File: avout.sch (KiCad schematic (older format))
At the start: 53 parts, among them CN6 AUDIO_VIDEO, M1 Modulator, Q3 2SC1815, Q81 2SC1815, Q82 2SC1815

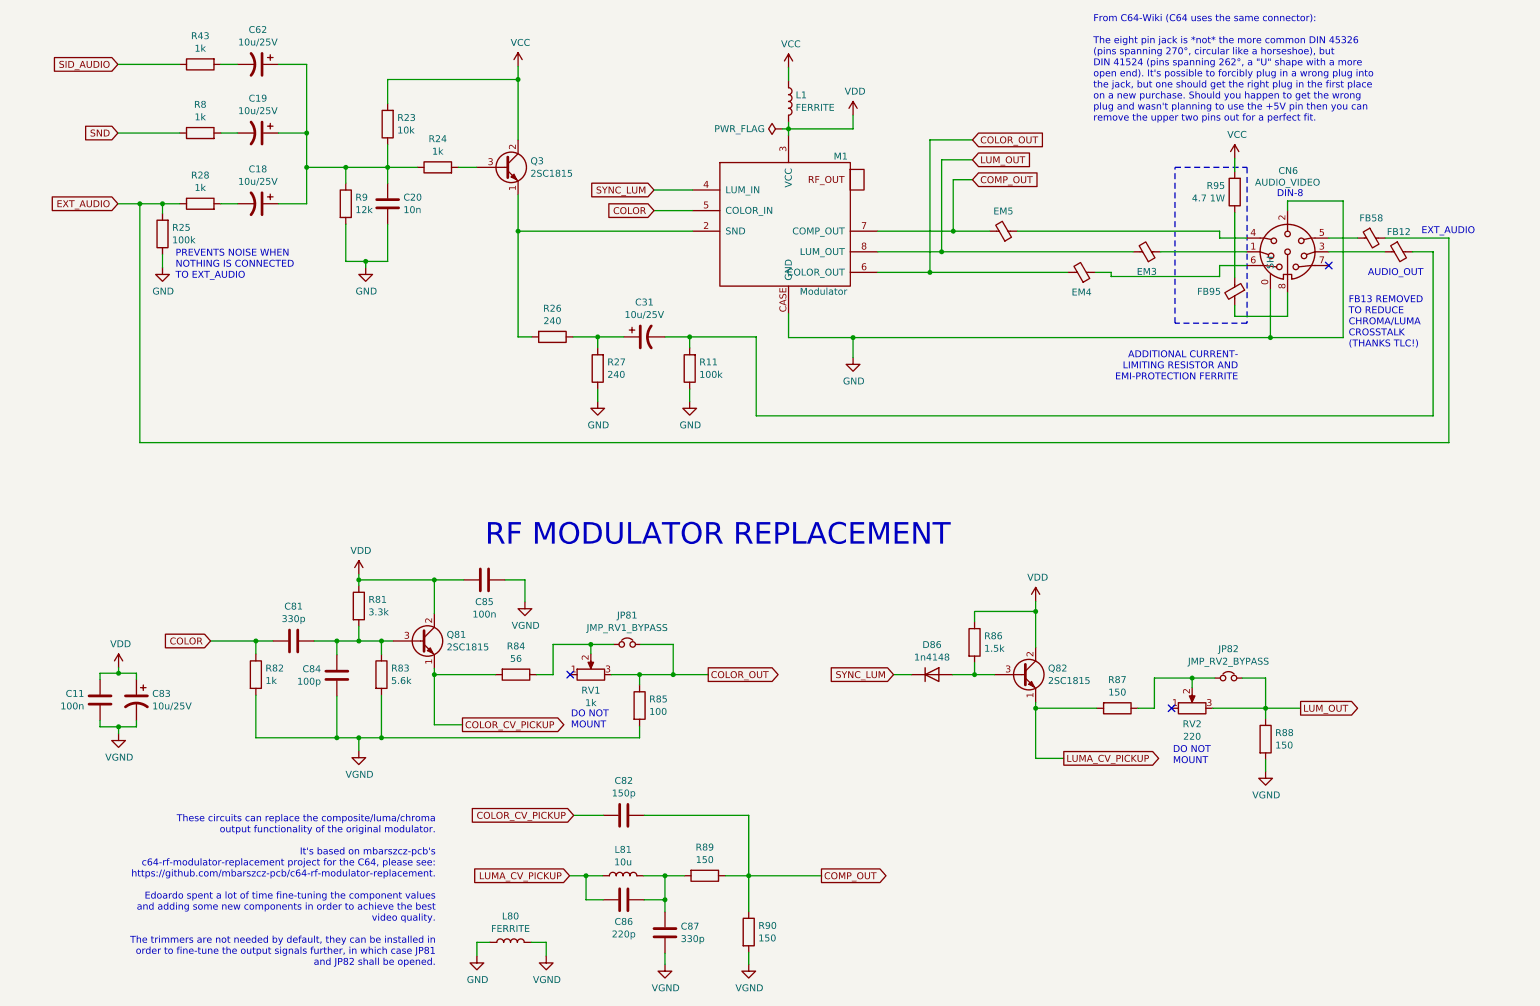
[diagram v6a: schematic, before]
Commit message: New composite video circuit
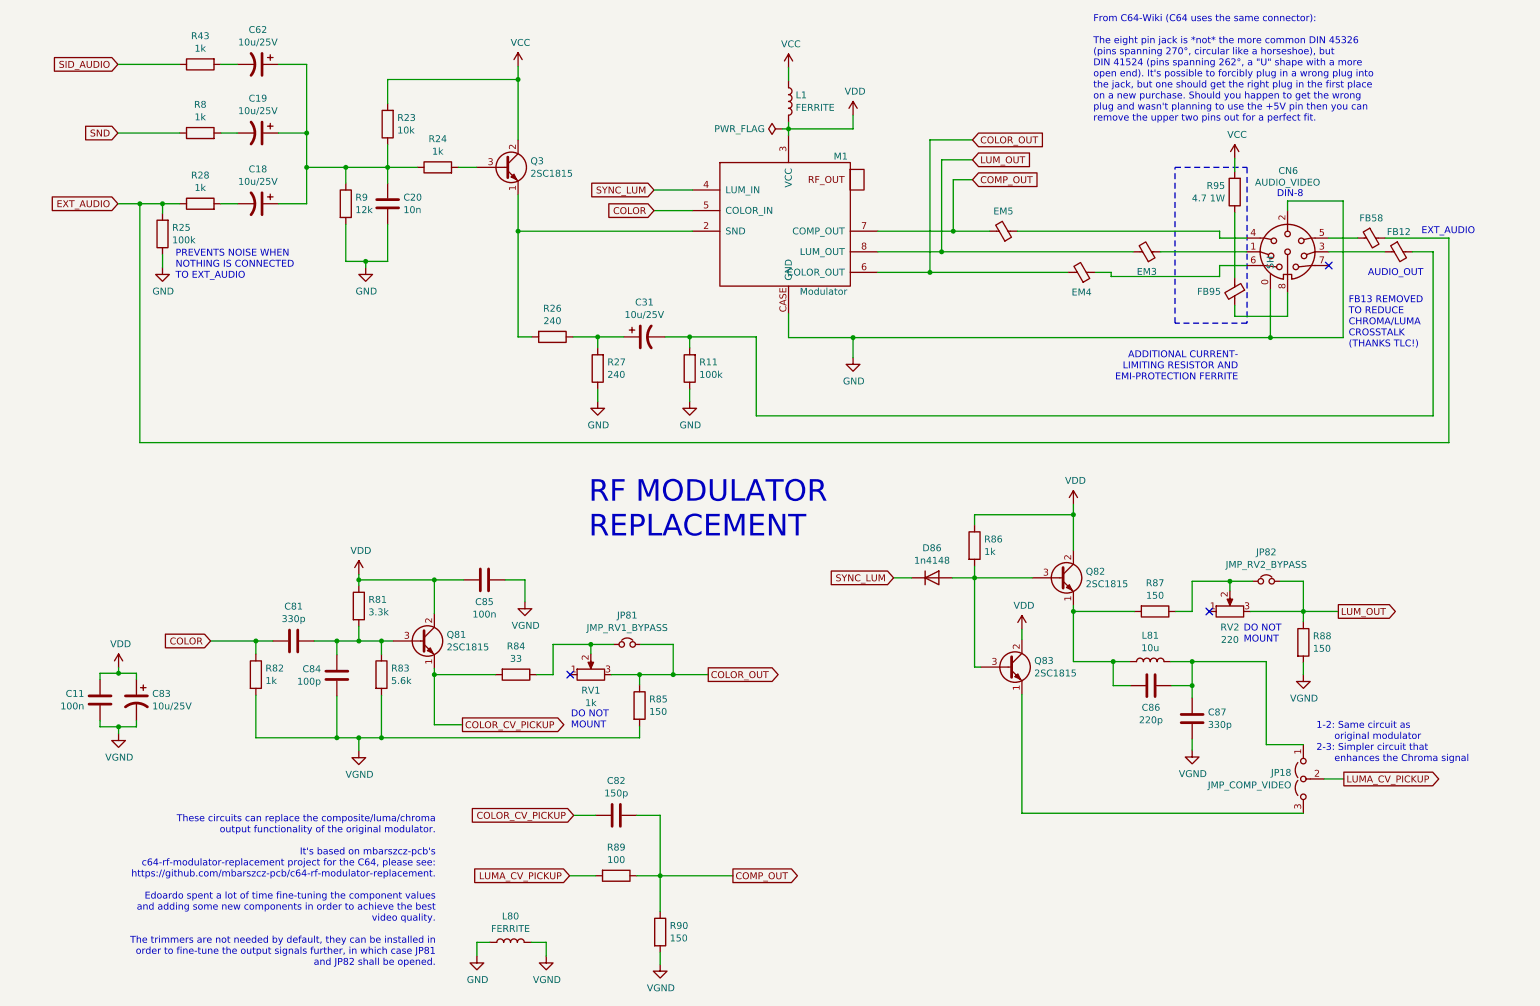
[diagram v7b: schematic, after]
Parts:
- added JP18: JMP_COMP_VIDEO, Jumper:SolderJumper-3_P1.3mm_Open_RoundedPad1.0x1.5mm, symbol Jumper:Jumper_3_Open
- added Q83: 2SC1815, Package_TO_SOT_THT:TO-92_Inline_Wide, symbol Transistor_BJT:2SC1815
- R84: value 56 -> 33
- R85: value 100 -> 150
- R86: value 1.5k -> 1k
- R89: value 150 -> 100
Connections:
- net LUMA_CV_PICKUP: now also R89.2, JP18.2 (C); no longer C86.2, L81.1, Q82.1 (E), R87.2
- net VDD: now also Q83.2 (C)
- net at D86.2 (A), Q82.3 (B), R86.2: now also Q83.3 (B)
- net at C86.1, C87.2, L81.2: now also JP18.1 (A); no longer R89.2
- new net: C86.2, L81.1, Q82.1 (E), R87.2
- new net: JP18.3 (B), Q83.1 (E)
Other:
- note added: "1-2: Same circuit as\n original modulator\n2-3: Simpler circuit that\n enhances the Chroma signal"
- note added: "RF MODULATOR\nREPLACEMENT"
- note removed: "RF MODULATOR REPLACEMENT"
- moved on the sheet: C82, C86, C87, D86, JP82, L81, Q82, R86, R87, R88, R89, R90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

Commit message: Fix some P/Ns
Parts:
- EM3, EM4, EM5: value DSS1NB32A271Q91A -> 270p; MouserPN (none) -> DSS1NB32A271Q91A
- FB12, FB58, FB95: value DSS1NB32A271Q91A -> FERRITE; MouserPN (none) -> 623-2743015112
- L81: MouserPN 542-78F100-RC -> 871-B78108E1103K000
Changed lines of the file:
@@
 P 10455 2315
 F 0 "FB12" V 10310 2315 50  0000 C CNN
-F 1 "DSS1NB32A271Q91A" H 10555 2270 50  0001 L CNN
+F 1 "FERRITE" H 10555 2270 50  0001 L CNN
 F 2 "LittleSixteen:EMI_Filter" V 10385 2315 50  0001 C CNN
 F 3 "~" H 10455 2315 50  0001 C CNN
+F 4 "623-2743015112" H 10455 2315 50  0001 C CNN "MouserPN"
 	1    10455 2315
 	0    -1   1    0
@@
 P 10255 2215
 F 0 "FB58" V 10110 2215 50  0000 C CNN
-F 1 "DSS1NB32A271Q91A" H 10355 2170 50  0001 L CNN
+F 1 "FERRITE" H 10355 2170 50  0001 L CNN
 F 2 "LittleSixteen:EMI_Filter" V 10185 2215 50  0001 C CNN
 F 3 "~" H 10255 2215 50  0001 C CNN
+F 4 "623-2743015112" H 10255 2215 50  0001 C CNN "MouserPN"
 	1    10255 2215
 	0    -1   1    0
@@
 F 2 "Inductor_THT:L_Axial_L7.0mm_D3.3mm_P12.70mm_Horizontal_Fastron_MICC" H 8645 5300 50  0001 C CNN
 F 3 "~" H 8645 5300 50  0001 C CNN
-F 4 "542-78F100-RC" H 8645 5300 50  0001 C CNN "MouserPN"
+F 4 "871-B78108E1103K000" H 8645 5300 50  0001 C CNN "MouserPN"
 	1    8645 5300
 	0    -1   -1   0
@@
 P 9260 2605
 F 0 "FB95" H 9360 2605 50  0000 L CNN
-F 1 "DSS1NB32A271Q91A" H 9360 2560 50  0001 L CNN
+F 1 "FERRITE" H 9360 2560 50  0001 L CNN
 F 2 "LittleSixteen:EMI_Filter" V 9190 2605 50  0001 C CNN
 F 3 "~" H 9260 2605 50  0001 C CNN
+F 4 "623-2743015112" H 9260 2605 50  0001 C CNN "MouserPN"
 	1    9260 2605
 	-1   0    0    -1
@@
 P 7575 2165
 F 0 "EM5" V 7720 2165 50  0000 C CNN
-F 1 "DSS1NB32A271Q91A" H 7675 2120 50  0001 L CNN
+F 1 "270p" H 7675 2120 50  0001 L CNN
 F 2 "LittleSixteen:EMI_Filter" V 7505 2165 50  0001 C CNN
 F 3 "~" H 7575 2165 50  0001 C CNN
+F 4 "DSS1NB32A271Q91A" H 7575 2165 50  0001 C CNN "MouserPN"
 	1    7575 2165
 	0    1    -1   0
@@
 P 8145 2465
 F 0 "EM4" V 8000 2465 50  0000 C CNN
-F 1 "DSS1NB32A271Q91A" H 8245 2420 50  0001 L CNN
+F 1 "270p" H 8245 2420 50  0001 L CNN
 F 2 "LittleSixteen:EMI_Filter" V 8075 2465 50  0001 C CNN
 F 3 "~" H 8145 2465 50  0001 C CNN
+F 4 "DSS1NB32A271Q91A" H 8145 2465 50  0001 C CNN "MouserPN"
 	1    8145 2465
 	0    1    -1   0
@@
 P 8620 2315
 F 0 "EM3" V 8475 2315 50  0000 C CNN
-F 1 "DSS1NB32A271Q91A" H 8720 2270 50  0001 L CNN
+F 1 "270p" H 8720 2270 50  0001 L CNN
 F 2 "LittleSixteen:EMI_Filter" V 8550 2315 50  0001 C CNN
 F 3 "~" H 8620 2315 50  0001 C CNN
+F 4 "DSS1NB32A271Q91A" H 8620 2315 50  0001 C CNN "MouserPN"
 	1    8620 2315
 	0    1    -1   0
